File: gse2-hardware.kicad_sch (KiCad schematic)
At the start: 66 parts, among them J1 PJ-002A, J16 ARM, J17 ALARM, J2 PJ-002A, J3 ARM Cortex Debug, J33 AI_Ports, J34 Misc_Ports, J4 USB-C, Q1 DMP3099L, Q15 DMG3402L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

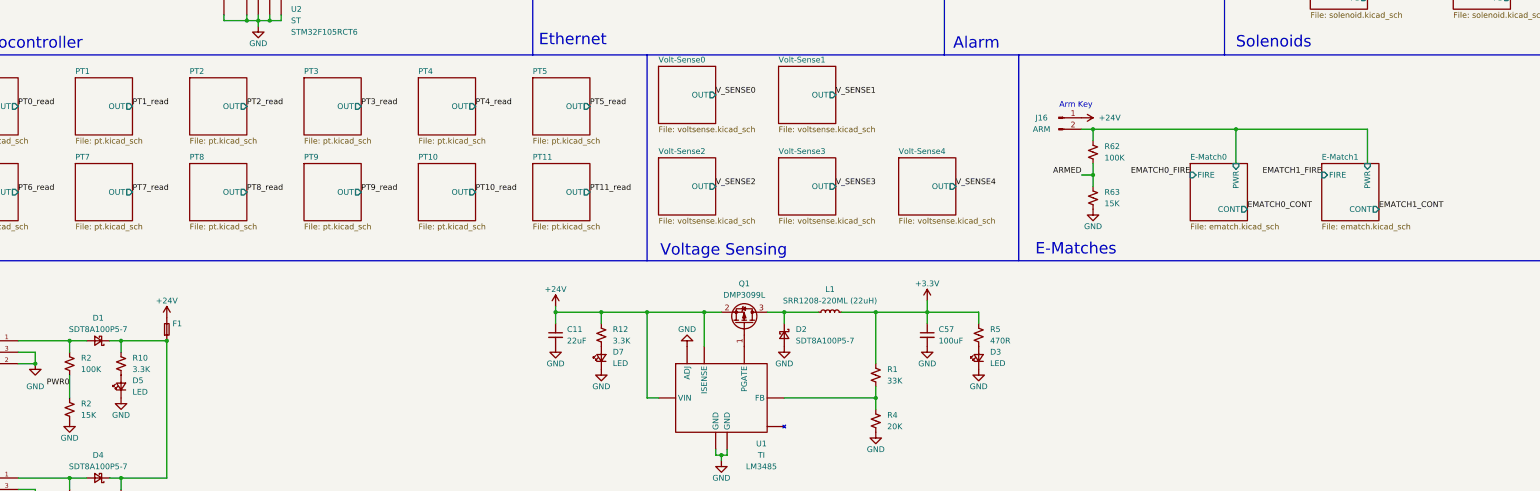
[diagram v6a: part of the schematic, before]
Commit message: Subsystem level layout done (prelim)
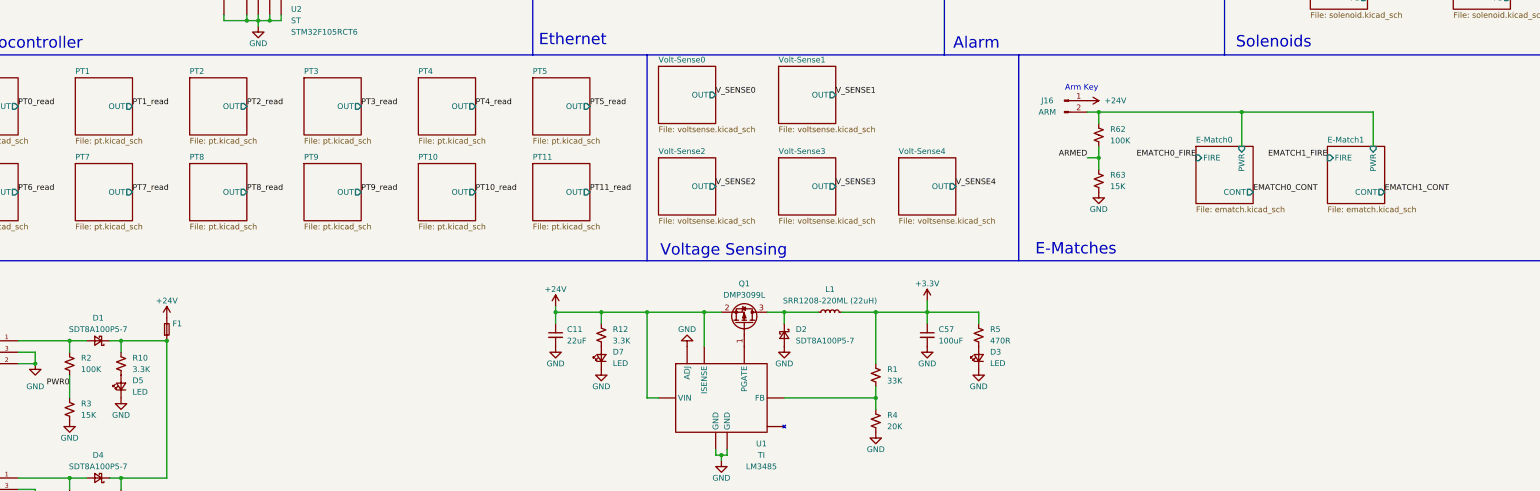
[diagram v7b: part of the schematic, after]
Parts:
- removed R2: 15K, Resistor_SMD:R_0402_1005Metric, symbol Device:R_Small_US
- added R3: 15K, Resistor_SMD:R_0603_1608Metric, symbol Device:R_Small_US
- C10, C2, C3, C4, C44, C5, C6, C7, C8, C9: footprint Capacitor_SMD:C_0402_1005Metric -> Capacitor_SMD:C_0603_1608Metric
- C11, C45, C46, C47, C48, C57, C69, C70: footprint Capacitor_SMD:C_1206_3216Metric -> Capacitor_SMD:C_0603_1608Metric
- R1, R10, R104, R12, R15, R16, R2, R4, R5, R62, R63, R64, R65, R7, R8, R82, R83, R9: footprint Resistor_SMD:R_0402_1005Metric -> Resistor_SMD:R_0603_1608Metric
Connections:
- net GND: now also R3.1
- net PWR0: now also R3.2
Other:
- moved on the sheet: J16, R62, R63
